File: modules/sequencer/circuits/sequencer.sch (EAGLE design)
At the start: 35 parts, among them IC2 LM324N

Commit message: sequencer design
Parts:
- added 1K, 1K1, 1K2, R23: 1k, adafruit:R-US_0207/12
- added 2N4400: (no value), transistor-neu-to92:2N4401-NPN-TO92-EBC
- added DAISY_CHAIN, INPUTS: (no value), pinhead:PINHD-1X6
- added MPS2907: (no value), transistor:MPS2907A-PNP-TO92-CBE
- added R20: 10k, adafruit:R-US_0207/12
- added R21: 100k, adafruit:R-US_0207/12
- added RESET_BUTTON: (no value), pinhead:PINHD-1X2
- added SPLIT_SELECT: (no value), pinhead:PINHD-2X3
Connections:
- new net COUNTER_POWER: CD4017G2.P$V+, MPS2907.C
- new net HALF_STEP: 1K1.2, CD4163G$1.Q4, R23.2
- new net N$2: CD4163G$1.PE, R20.2
- new net N$30: 1K.1, 2N4400.C, SPLIT_SELECT.3
- new net N$31: 2N4400.B, R23.1
- new net N$32: POWER.1, RESET_BUTTON.1
- new net N$36: 1K1.1, SPLIT_SELECT.5
- new net N$37: MPS2907.B, SPLIT_SELECT.2, SPLIT_SELECT.4, SPLIT_SELECT.6
- new net N$38: 1K2.1, SPLIT_SELECT.1
- net -12V: now also DAISY_CHAIN.4, INPUTS.4
- net 12V: now also DAISY_CHAIN.3, INPUTS.3
- net 3.3V: now also 2N4400.E, CD4017G1.RES, CD4163P.VSS, DAISY_CHAIN.6, INPUTS.6
- net 5V: now also 1K.2, 1K2.2, CD4163P.VDD, DAISY_CHAIN.5, INPUTS.5, MPS2907.E, R20.1, R21.1, RESET_BUTTON.2; no longer CD4017G2.P$V+, POWER.1
- net CLK_IN: now also CD4163G$1.CLK, DAISY_CHAIN.1, INPUTS.1
- net N$10: now also R19.2; no longer R1.2
- net N$3: now also R1.2; no longer R19.2
- net N$4: now also R13.2; no longer R18.2
- net N$5: now also R14.2; no longer R17.2
- net N$6: now also R15.2; no longer R16.2
- net N$7: now also R16.2; no longer R15.2
- net N$8: now also R17.2; no longer R14.2
- net N$9: now also R18.2; no longer R13.2
- net RESET: now also CD4163G$1.!CLEAR, CD4163G$1.!LOAD, R21.2; no longer CD4017G1.RES
- net START_STOP: now also DAISY_CHAIN.2, INPUTS.2
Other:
- note added: "Counts from 0 to 15. To split steps accross 2 daisy-chained sequencers"
- note added: "jumper on 1&2: counter always enabled 3&4: counter off from steps 0-7 5&6: counter off from steps 8-15"
- note added: "on-mom switch. or jumper to leave out reset functionality"
- moved on the sheet: CD4163, CD4163P

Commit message: Sync
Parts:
- removed C3: 2.2uf, adafruit:CPOL-USE2,5-6E
- removed C4: 1uf, adafruit:CPOL-USE2,5-6E
- removed INPUTS: (no value), pinhead:PINHD-1X6
- removed LM7905: (no value), linear:7905T
- removed POWER: (no value), pinhead:PINHD-1X4
- added 1: 4017N, 40xx:4017N
- added D10, D11, D12, D13, D14, D15, D16, D9: 1N4004, adafruit:1N4004
- added INPUTS1: (no value), pinhead:PINHD-1X6
- added R40, R56: 10k, SparkFun-Resistors:10KOHM-HORIZ-1/4W-1%
- added R41, R42, R43, R44, R45, R46, R47, R48, R49, R50, R51, R52, R53, R54, R55: 1k, SparkFun-Resistors:10KOHM-HORIZ-1/4W-1%
- added WIDTH_SELECTION1: (no value), pinhead:PINHD-2X7
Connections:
- removed net -5V: C4.-, IC2P.V-, LM7905.VO
- removed net START_STOP: CD4017G1.ENA, DAISY_CHAIN.2, INPUTS.2
- removed net VDD: C3.-, LM7905.VI
- new net DIV_CLK: CD4017G1.CLK, D10.C, D11.C, D12.C, D9.C, DAISY_CHAIN.1, R40.1
- new net GATE_OUT: R47.2, R48.2, R56.1
- new net GND: 1A.ENA, 1P.VSS
- new net GNDA: R40.2, R56.2, WIDTH_SELECTION1.10, WIDTH_SELECTION1.12, WIDTH_SELECTION1.14, WIDTH_SELECTION1.2, WIDTH_SELECTION1.4, WIDTH_SELECTION1.6, WIDTH_SELECTION1.8
- new net N$56: 1A.Q8, 1A.RES
- new net N$57: 1A.Q0, D16.A, D9.A
- new net N$58: 1A.Q1, D10.A, D13.A
- new net N$59: 1A.Q2, D11.A, D14.A
- new net N$60: 1A.Q3, D12.A, D15.A
- new net N$61: 1A.Q7, R48.1
- new net N$62: R41.2, R47.1, R49.2, WIDTH_SELECTION1.13
- new net N$63: R41.1, R42.2, R50.2, WIDTH_SELECTION1.11
- new net N$64: 1A.Q4, R51.1
- new net N$65: R43.1, R44.2, R52.2, WIDTH_SELECTION1.7
- new net N$66: R44.1, R45.2, R53.2, WIDTH_SELECTION1.5
- new net N$67: R45.1, R46.2, R54.2, WIDTH_SELECTION1.3
- new net N$68: R46.1, R55.2, WIDTH_SELECTION1.1
- new net N$69: 1A.Q6, R49.1
- new net N$70: 1A.Q5, R50.1
- new net N$71: R42.1, R43.2, R51.2, WIDTH_SELECTION1.9
- new net N$72: D15.C, R52.1
- new net N$73: D14.C, R53.1
- new net N$74: D13.C, R54.1
- new net N$75: D16.C, R55.1
- net -12V: now also IC2P.V-, INPUTS1.3; no longer INPUTS.4, POWER.3
- net 12V: now also IC2P.V+, INPUTS1.2; no longer INPUTS.3, POWER.2
- net 3.3V: now also INPUTS1.4; no longer C3.+, C4.+, INPUTS.6, LM7905.GND, POWER.4
- net 5V: now also 1P.VDD; no longer IC2P.V+, INPUTS.5
- net CLK_IN: now also 1A.CLK, INPUTS1.5; no longer CD4017G1.CLK, DAISY_CHAIN.1, INPUTS.1
- net N$32: now also INPUTS1.1; no longer POWER.1
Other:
- note added: "Input clock divided by 8"
- note added: "Jumper setting changes clock width: no jumper: 100% (always high) 1&2: 7/8 duty cycle 3&4: 6/8 duty cycle 5&6: 5/8 duty cycle 7&8: 4/8 duty cycle 9&10: 3/8 duty cycle 11&12: 2/8 duty cycle 13&14: 1/8 duty cycle"
- moved on the sheet: 2N4400, CD4017G1, CD4017G2, CD4163, CD4163P, DAISY_CHAIN, LED1, LED2, LED3, LED4, LED5, LED6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

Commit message: divider
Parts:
- removed 1: 4017N, 40xx:4017N
- removed D10, D11, D12, D13, D14, D15, D16, D9: 1N4004, adafruit:1N4004
- removed R40, R56: 10k, SparkFun-Resistors:10KOHM-HORIZ-1/4W-1%
- removed R41, R42, R43, R44, R45, R46, R47, R48, R49, R50, R51, R52, R53, R54, R55: 1k, SparkFun-Resistors:10KOHM-HORIZ-1/4W-1%
- removed WIDTH_SELECTION1: (no value), pinhead:PINHD-2X7
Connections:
- removed net DIV_CLK: CD4017G1.CLK, D10.C, D11.C, D12.C, D9.C, DAISY_CHAIN.1, R40.1
- removed net GATE_OUT: R47.2, R48.2, R56.1
- removed net GND: 1A.ENA, 1P.VSS
- removed net GNDA: R40.2, R56.2, WIDTH_SELECTION1.10, WIDTH_SELECTION1.12, WIDTH_SELECTION1.14, WIDTH_SELECTION1.2, WIDTH_SELECTION1.4, WIDTH_SELECTION1.6, WIDTH_SELECTION1.8
- removed net N$56: 1A.Q8, 1A.RES
- removed net N$57: 1A.Q0, D16.A, D9.A
- removed net N$58: 1A.Q1, D10.A, D13.A
- removed net N$59: 1A.Q2, D11.A, D14.A
- removed net N$60: 1A.Q3, D12.A, D15.A
- removed net N$61: 1A.Q7, R48.1
- removed net N$62: R41.2, R47.1, R49.2, WIDTH_SELECTION1.13
- removed net N$63: R41.1, R42.2, R50.2, WIDTH_SELECTION1.11
- removed net N$64: 1A.Q4, R51.1
- removed net N$65: R43.1, R44.2, R52.2, WIDTH_SELECTION1.7
- removed net N$66: R44.1, R45.2, R53.2, WIDTH_SELECTION1.5
- removed net N$67: R45.1, R46.2, R54.2, WIDTH_SELECTION1.3
- removed net N$68: R46.1, R55.2, WIDTH_SELECTION1.1
- removed net N$69: 1A.Q6, R49.1
- removed net N$70: 1A.Q5, R50.1
- removed net N$71: R42.1, R43.2, R51.2, WIDTH_SELECTION1.9
- removed net N$72: D15.C, R52.1
- removed net N$73: D14.C, R53.1
- removed net N$74: D13.C, R54.1
- removed net N$75: D16.C, R55.1
- net 5V: no longer 1P.VDD
- net CLK_IN: now also CD4017G1.CLK, DAISY_CHAIN.1; no longer 1A.CLK
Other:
- note removed: "Input clock divided by 8"
- note removed: "Jumper setting changes clock width: no jumper: 100% (always high) 1&2: 7/8 duty cycle 3&4: 6/8 duty cycle 5&6: 5/8 duty cycle 7&8: 4/8 duty cycle 9&10: 3/8 duty cycle 11&12: 2/8 duty cycle 13&14: 1/8 duty cycle"

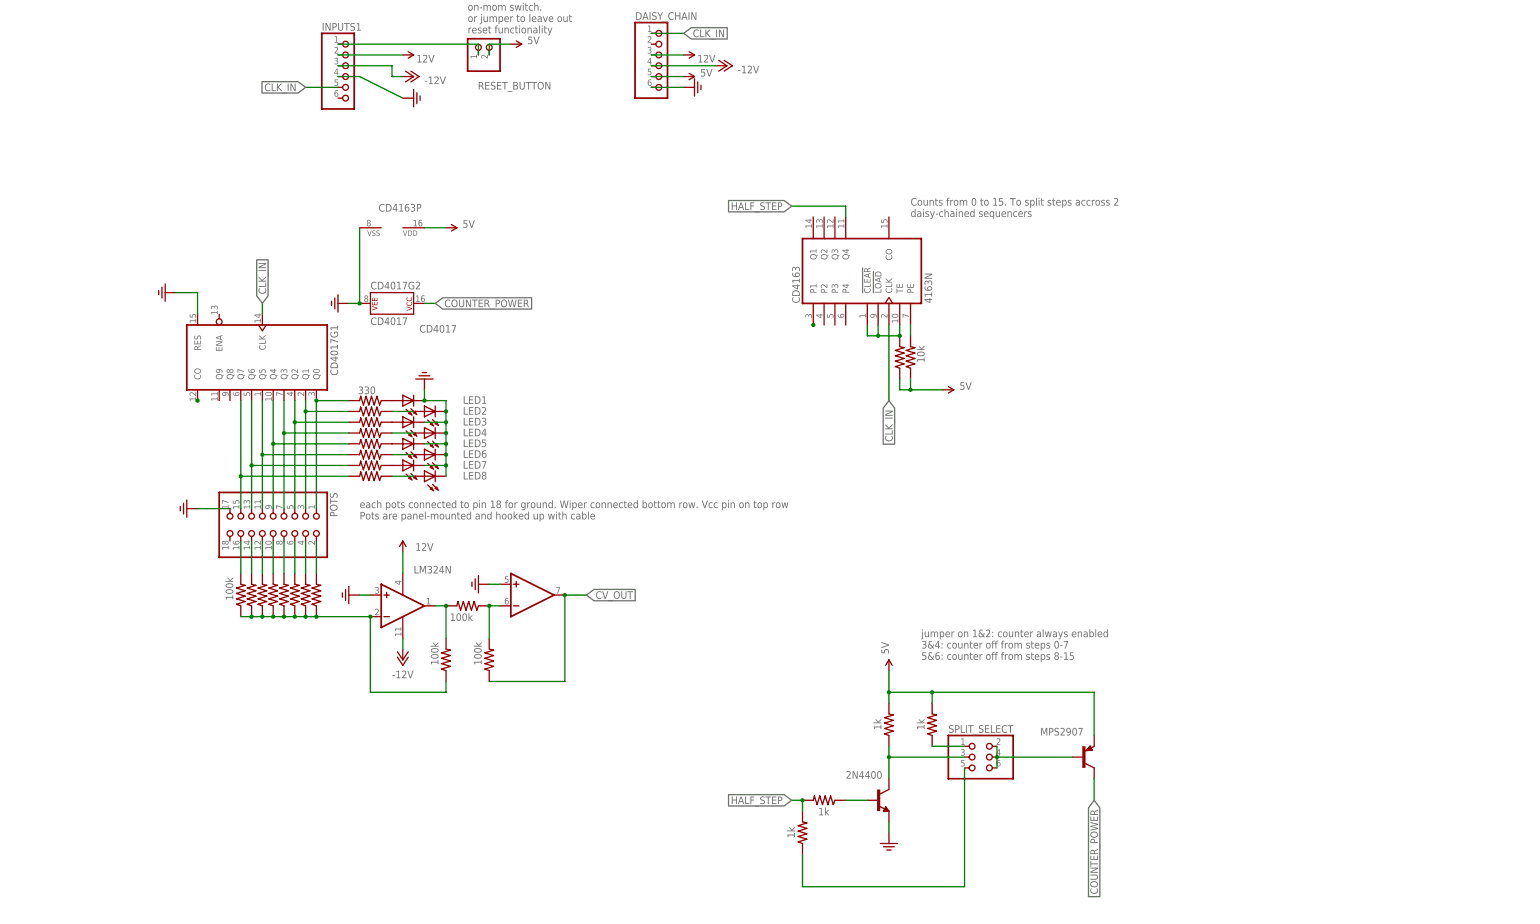
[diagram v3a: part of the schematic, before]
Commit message: Sequencer design complete
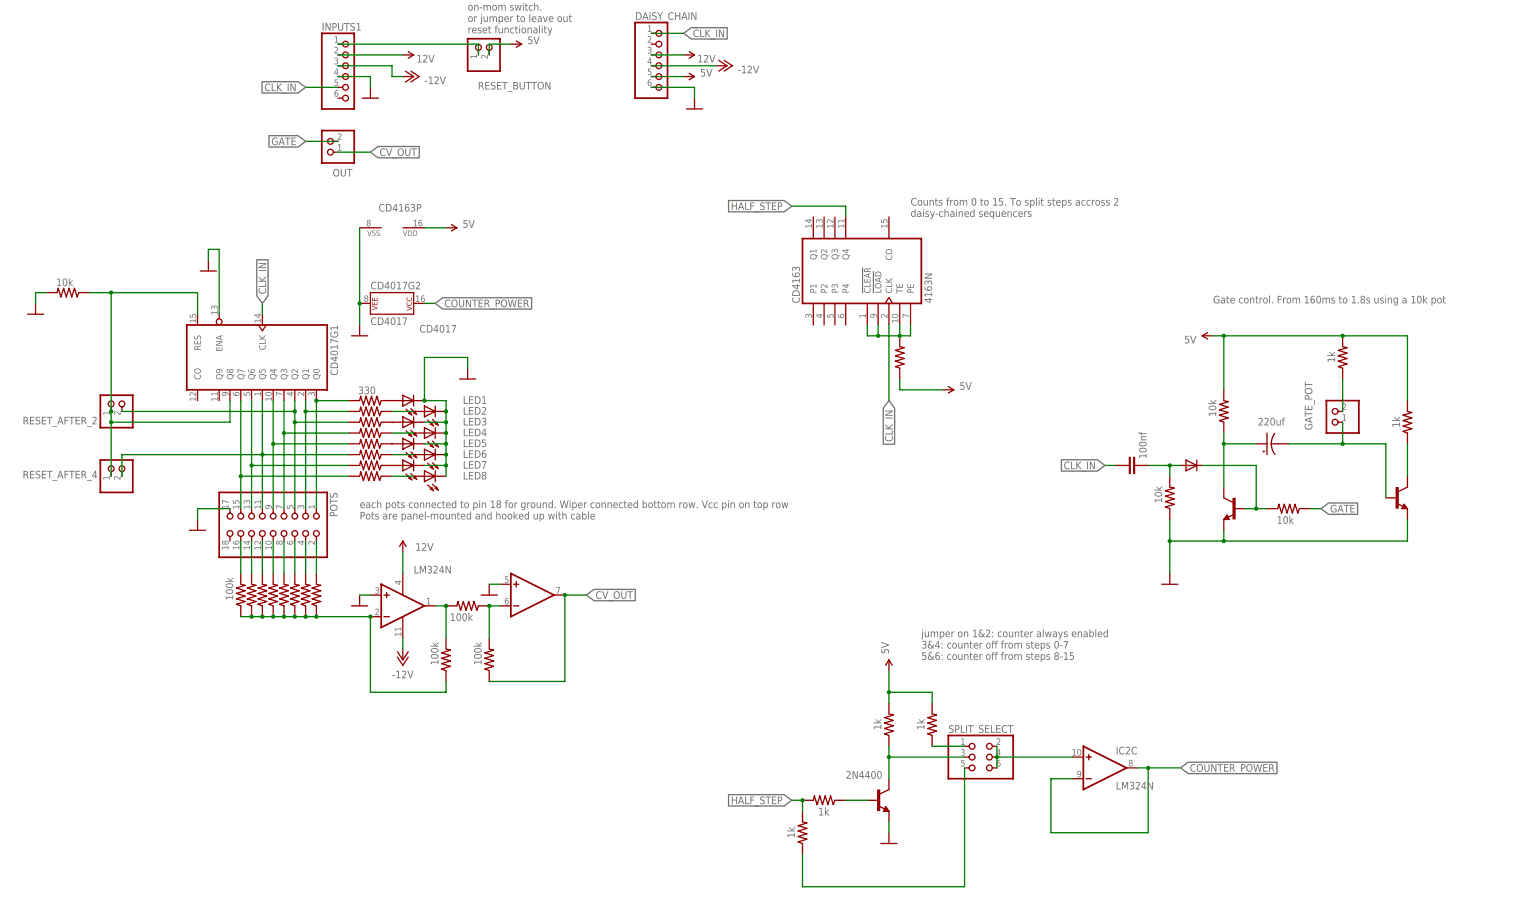
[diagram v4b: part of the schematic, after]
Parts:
- removed MPS2907: (no value), transistor:MPS2907A-PNP-TO92-CBE
- added 1K3, 1K4: 1k, adafruit:R-US_0207/12
- added 2N1, 2N2: (no value), transistor-neu-to92:2N4401-NPN-TO92-EBC
- added C2: 220uf, rcl:CPOL-USE2,5-6E
- added C3: 100nf, rcl:C-EU025-024X044
- added D1: 1N4004, adafruit:1N4004
- added GATE_POT, OUT, RESET_AFTER_2, RESET_AFTER_4: (no value), pinhead:PINHD-1X2
- added R22, R24, R25: 10k, adafruit:R-US_0207/12
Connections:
- removed net 3.3V: 2N4400.E, CD4017G1.RES, CD4017G2.P$V-, CD4163P.VSS, DAISY_CHAIN.6, IC2A.+IN, IC2B.+IN, INPUTS1.4, LED1.C, LED2.C, LED3.C, LED4.C, LED5.C, LED6.C, LED7.C, LED8.C, POTS.17
- new net GATE: OUT.2, R24.1
- new net GND: 2N1.E, 2N2.E, 2N4400.E, CD4017G1.ENA, CD4017G2.P$V-, CD4163P.VSS, DAISY_CHAIN.6, IC2A.+IN, IC2B.+IN, INPUTS1.4, LED1.C, LED2.C, LED3.C, LED4.C, LED5.C, LED6.C, LED7.C, LED8.C, POTS.17, R20.1, R22.2
- new net N$35: 2N2.B, D1.C, R24.2
- new net N$39: 2N2.C, C2.+, R25.1
- new net N$40: 1K3.1, 2N1.C
- new net N$41: 1K4.1, GATE_POT.2
- new net N$42: 2N1.B, C2.-, GATE_POT.1
- net 5V: now also 1K3.2, 1K4.2, R25.2; no longer MPS2907.E, R20.1
- net CLK_IN: now also C3.1
- net COUNTER_POWER: now also IC2C.-IN, IC2C.OUT; no longer MPS2907.C
- net CV_OUT: now also OUT.1
- net N$1: now also CD4017G1.Q8, CD4017G1.RES, R22.1, RESET_AFTER_2.1, RESET_AFTER_4.1; no longer CD4017G1.CO, CD4163G$1.P1
- net N$2: now also C3.2, D1.A; no longer CD4163G$1.PE
- net N$37: now also IC2C.+IN; no longer MPS2907.B
- net N$5: now also RESET_AFTER_2.2
- net N$8: now also RESET_AFTER_4.2
- net RESET: now also CD4163G$1.PE
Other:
- note added: "Gate control. From 160ms to 1.8s using a 10k pot"

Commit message: Seq board
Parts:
- removed 1K, 1K2: 1k, adafruit:R-US_0207/12
- removed 2N1, 2N4400: (no value), transistor-neu-to92:2N4401-NPN-TO92-EBC
- removed C3: 100nf, rcl:C-EU025-024X044
- removed CD4163: 4163N, 40xx:4163N
- removed DAISY_CHAIN: (no value), pinhead:PINHD-1X6
- removed R24, R25: 10k, adafruit:R-US_0207/12
- removed SPLIT_SELECT: (no value), pinhead:PINHD-2X3
- added C1: 0.01uf, rcl:C-EU025-024X044
- added C4: 0.1uf, rcl:C-EU025-024X044
- added IC1: LM555N, adafruit:LM555N
- added LED9: (no value), adafruit:LED5MM
- 1K1: value 1k -> 100k
- 1K4: value 1k -> 10k
- D1: device adafruit:1N4004 -> diode:1N4004
- R21: value 100k -> 100
- R23: value 1k -> 330
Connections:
- removed net COUNTER_POWER: CD4017G2.P$V+, IC2C.-IN, IC2C.OUT
- removed net HALF_STEP: 1K1.2, CD4163G$1.Q4, R23.2
- removed net N$37: IC2C.+IN, SPLIT_SELECT.2, SPLIT_SELECT.4, SPLIT_SELECT.6
- removed net N$38: 1K2.1, SPLIT_SELECT.1
- removed net N$39: 2N2.C, C2.+, R25.1
- removed net N$40: 1K3.1, 2N1.C
- removed net N$41: 1K4.1, GATE_POT.2
- removed net N$42: 2N1.B, C2.-, GATE_POT.1
- removed net RESET: CD4163G$1.!CLEAR, CD4163G$1.!LOAD, CD4163G$1.PE, CD4163G$1.TE, R21.2
- new net N$33: C4.1, D1.A, IC1.TR, R20.1
- new net N$34: C1.1, IC1.CV
- net -12V: no longer DAISY_CHAIN.4
- net 12V: no longer DAISY_CHAIN.3
- net 5V: now also C2.+, CD4017G2.P$V+, D1.C, IC1.R, IC1.V+, INPUTS1.1, R20.2, RESET_BUTTON.1; no longer 1K.2, 1K2.2, 1K3.2, CD4163P.VDD, DAISY_CHAIN.5, R21.1, R25.2, RESET_BUTTON.2
- net CLK_IN: now also 2N2.B; no longer C3.1, CD4163G$1.CLK, DAISY_CHAIN.1
- net GATE: now also 1K1.2; no longer R24.1
- net GND: now also C1.2, GATE_POT.1, IC1.GND, R23.1; no longer 2N1.E, 2N4400.E, CD4163P.VSS, DAISY_CHAIN.6, R20.1
- net N$1: now also RESET_BUTTON.2
- net N$10: no longer R19.2
- net N$2: now also 1K3.1, C4.2; no longer C3.2, D1.A, R20.2
- net N$3: no longer R1.2
- net N$30: now also LED9.C, R23.2; no longer 1K.1, 2N4400.C, SPLIT_SELECT.3
- net N$31: now also GATE_POT.2, R21.1; no longer 2N4400.B, R23.1
- net N$32: now also 1K3.2, 1K4.1, 2N2.C; no longer INPUTS1.1, RESET_BUTTON.1
- net N$35: now also C2.-, IC1.DIS, IC1.THR, R21.2; no longer 2N2.B, D1.C, R24.2
- net N$36: now also IC1.Q, LED9.A; no longer SPLIT_SELECT.5
- net N$4: no longer R13.2
- net N$5: no longer R14.2
- net N$6: no longer R15.2
- net N$7: no longer R16.2
- net N$8: no longer R17.2
- net N$9: no longer R18.2
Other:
- note added: "CV out will not be within the full range of 5V because of the output of the 4017. Ideally, everything would be powered from 12v and CV would be attenuated proportionally with the voltage measured before the POTs"
- note added: "differentiator"
- note added: "pulse generator"
- note added: "signal inverter"
- note added: "status led and ouput"
- note removed: "Counts from 0 to 15. To split steps accross 2 daisy-chained sequencers"
- note removed: "jumper on 1&2: counter always enabled 3&4: counter off from steps 0-7 5&6: counter off from steps 8-15"
- note removed: "on-mom switch. or jumper to leave out reset functionality"
- moved on the sheet: CD4017G1, CD4017G2, GATE_POT, INPUTS1, LED1, LED2, LED3, LED4, LED5, LED6, LED7, LED8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
